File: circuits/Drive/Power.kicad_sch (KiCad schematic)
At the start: 82 parts, among them J2 Conn_01x02_Pin, J3 Conn_01x02_Pin, J4 Conn_01x02_Pin, J5 Conn_01x02_Pin, J6 Conn_01x02_Pin, J7 USB_C_Receptacle_PowerOnly_6P, Q16 SSM6J808R, Q17 SSM6J808R, Q18 SSM3J332R, Q19 S8550, Q20 SSM3J332R, Q21 S8550, Q23 S8550, Q24 SSM3J332R, Q25 S8550, Q3 SSM3J332R, Q5 2N7002, Q8 2N7002, SW1 SW_SPDT_White, U1 AZ1117CH-3.3, U2 DCDC_TPSM336x5

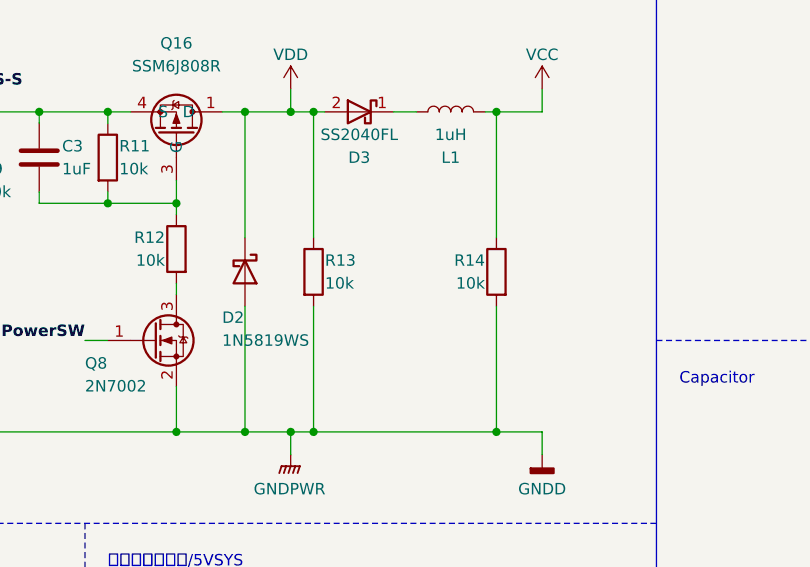
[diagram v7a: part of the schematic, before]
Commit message: 発注第2弾
RasPi発注
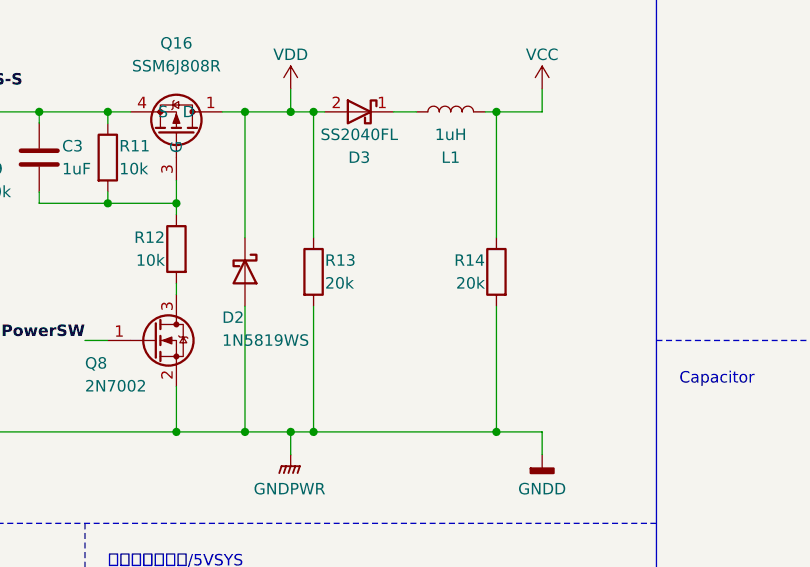
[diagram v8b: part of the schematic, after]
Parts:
- R13, R14: value 10k -> 20k
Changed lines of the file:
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@@
       (effects (font (size 1.27 1.27)) (justify left))
     )
-    (property "Value" "10k" (at 232.41 90.17 0)
+    (property "Value" "20k" (at 232.41 90.17 0)
       (effects (font (size 1.27 1.27)) (justify left))
     )
@@
       (effects (font (size 1.27 1.27)) (justify left))
     )
-    (property "Value" "10k" (at 250.19 90.17 0)
-      (effects (font (size 1.27 1.27)) (justify left))
-    )
+    (property "Value" "20k" (at 250.19 90.17 0)
+      (effects (font (size 1.27 1.27)) (justify left))
+    )
